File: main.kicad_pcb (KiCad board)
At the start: 2 copper layers, 58.4 x 76.2 mm, 56 parts, among them J1 USB_OTG, SW1 SW_Push, SW1 ~RST, SW2 SW_Push, U1 TM4C123GH6PM, U2 LM1117-3.3, Y1 Crystal-16MHz, Y2 Crystal-32.768KHz

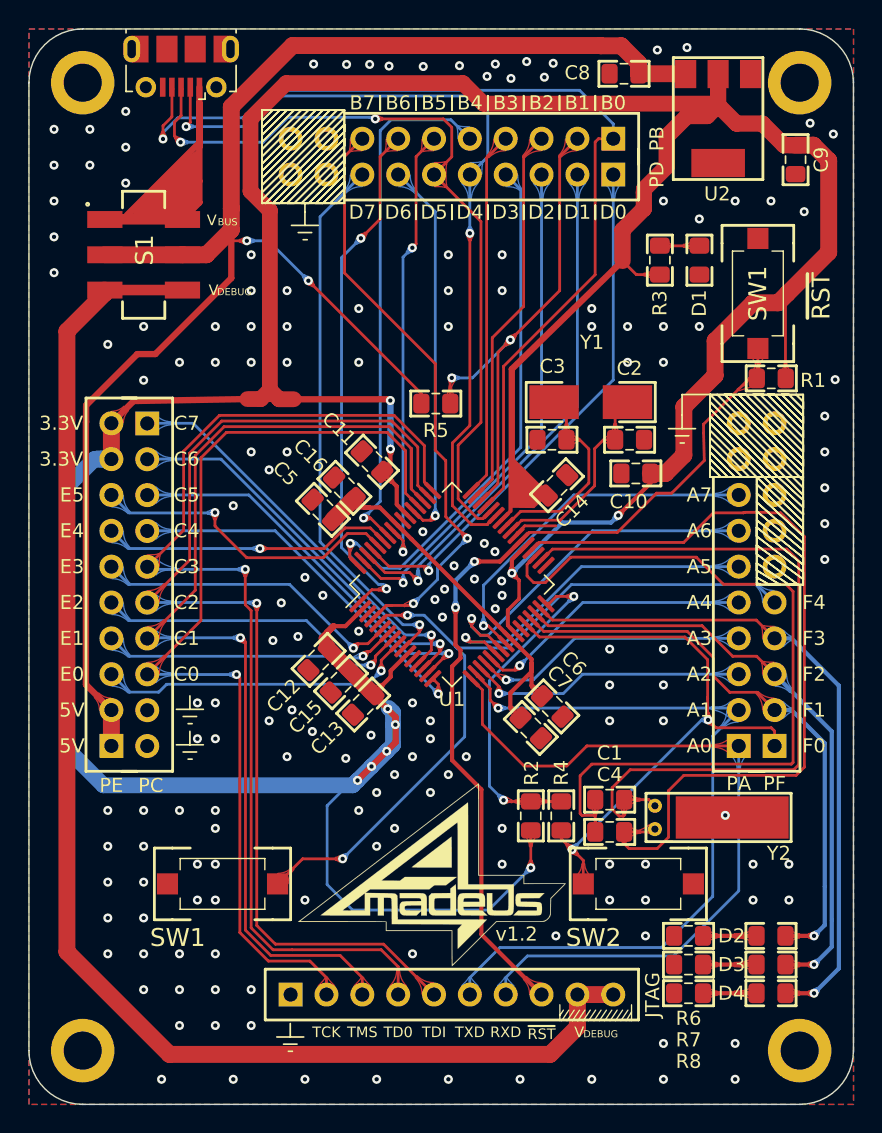
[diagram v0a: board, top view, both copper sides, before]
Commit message: Updated
Cập nhật lại điện trở treo cho JTAG
Thay thạch anh SMD thành loại dễ tìm hơn
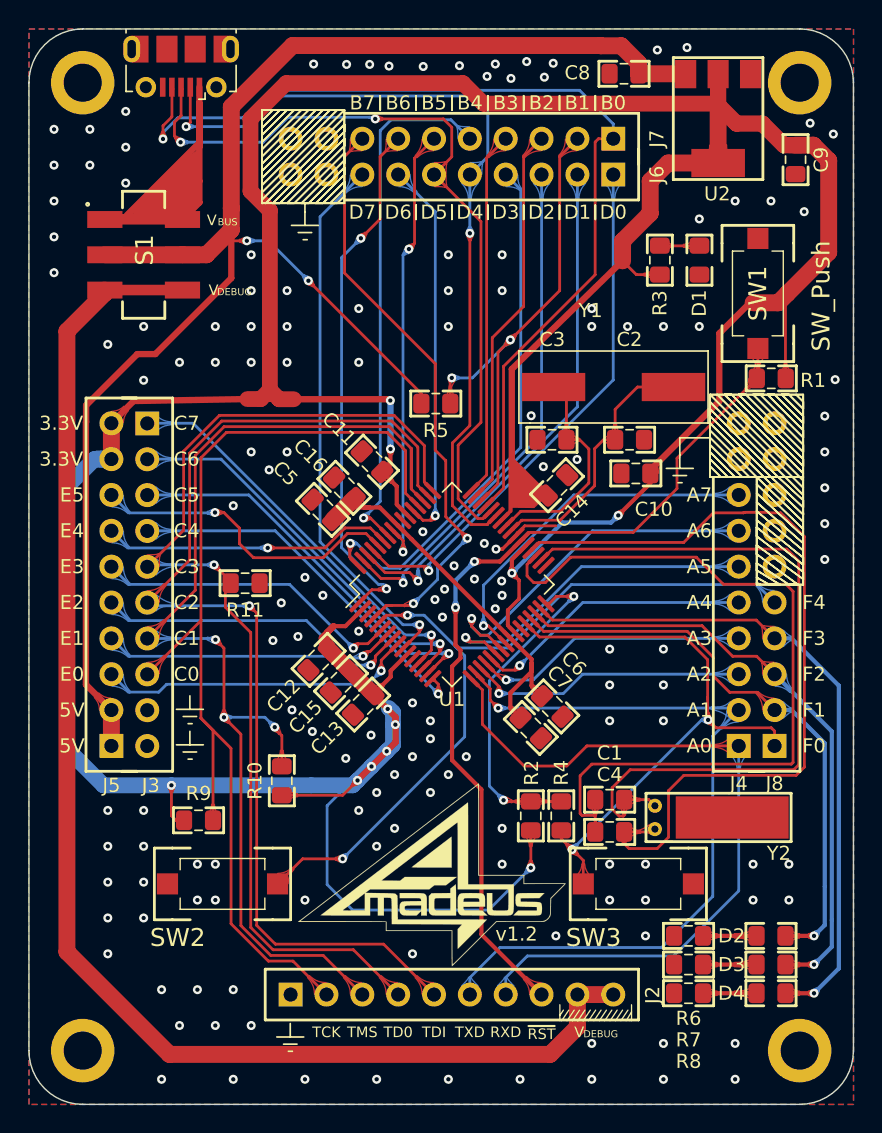
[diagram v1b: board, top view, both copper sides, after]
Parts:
- added R10: 10k, tm4c:R_0805_2012Metric_Pad1.15x1.40mm_HandSolder, F.Cu at (127.9, 112.2)
- added R11: 10k, tm4c:R_0805_2012Metric_Pad1.15x1.40mm_HandSolder, F.Cu at (125.3, 98.2)
- added R9: 10k, tm4c:R_0805_2012Metric_Pad1.15x1.40mm_HandSolder, F.Cu at (122.0, 115.0)
- C10: value 0.01pF -> 0.01uF
- SW1: value ~RST -> SW_Push
- Y1: footprint tm4c:Crystal_SMD_5032-2Pin_5.0x3.2mm_HandSoldering -> tm4c:Crystal_SMD_HC49-SD
- moved REF** 2.82 mm to (156.1, 89.1)
- moved Y1 1.93 mm to (151.4, 84.3)
- renumbered JTAG to J2, PC to J3, PA to J4, PE to J5, PD to J6, PB to J7, PF to J8, SW1 to SW2, SW2 to SW3
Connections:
- U1 pad 33: (no net) -> Net-(U1-Pad33)
- U2 pad 4: Earth -> +3V3
- Y2 pad 3: Earth -> (no net)
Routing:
- net +3V3: track 313.4 -> 323.1 mm, vias 10 -> 11
- net /PC0: track 70.3 -> 75.8 mm, vias 1 -> 0
- net /PC1: track 76.4 -> 81.4 mm, vias 1 -> 3
- net Net-(C2-Pad2): track 14.6 -> 18.8 mm
- net /PC3: track 77.8 -> 75.6 mm
- net Earth: track 3.15 -> 4.97 mm, vias 165 -> 152
- net Net-(C3-Pad1): track 14.4 -> 15.8 mm
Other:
- net class Default: via_dia 0.8 -> 0.64; via_drill 0.4 -> 0.3

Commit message: Updated
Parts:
- SW1: value SW_Push -> ~RST
- moved R9 0.81 mm to (122.8, 115.1)
- renumbered J2 to JTAG, J4 to PA, J7 to PB, J3 to PC, J6 to PD, J5 to PE, J8 to PF, SW2 to SW1, SW3 to SW2
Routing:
- net /PC0: track 75.8 -> 70.2 mm
- net +3V3: track 323.1 -> 322.1 mm

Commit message: Updated a little
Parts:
- removed the REF** at (128.5, 129.4)
- added REF**: Earth, tm4c:Earth, F.Cu at (151.4, 129.7)
- added REF**: Earth, tm4c:Earth, F.Cu at (128.5, 129.7)
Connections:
- JTAG pad 10: /VDEBUG -> Earth
- Y2 pad 3: (no net) -> Earth
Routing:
- net /VDEBUG: track 98.3 -> 95.8 mm
- net Earth: track 4.97 -> 3.21 mm, vias 152 -> 158
- net /PC0: track 70.2 -> 71.1 mm
- net +3V3: track 322.1 -> 322.9 mm
